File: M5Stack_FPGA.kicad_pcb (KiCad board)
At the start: 2 copper layers, 49.6 x 49.6 mm, 34 parts, among them J1 MBUS_BOTTOM, J2 MBUS_TOP, U1 BP35A1, U2 PCA9557

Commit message: Partially routed
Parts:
- removed JP1, JP2, JP3: Jumper_3_Bridged12, Jumper:SolderJumper-3_P1.3mm_Bridged12_Pad1.0x1.5mm
- added C10: 100n, Capacitor_SMD:C_0402_1005Metric, F.Cu at (36.5, 67.2)
- added C11: 100n, Capacitor_SMD:C_0402_1005Metric, F.Cu at (32.0, 67.2)
- added C13: 100n, Capacitor_SMD:C_0402_1005Metric, F.Cu at (38.5, 56.8)
- added C14: 100n, Capacitor_SMD:C_0402_1005Metric, F.Cu at (37.2, 62.2)
- added C15: 100n, Capacitor_SMD:C_0402_1005Metric, B.Cu at (29.9, 81.0)
- added C16: 100n, Capacitor_SMD:C_0402_1005Metric, F.Cu at (2.72, 27.6)
- added C17: 100n, Capacitor_SMD:C_0402_1005Metric, F.Cu at (27.8, 56.8)
- added C18: 100n, Capacitor_SMD:C_0402_1005Metric, F.Cu at (32.0, 56.8)
- added C19: 100n, Capacitor_SMD:C_0402_1005Metric, F.Cu at (26.5, 61.8)
- added C2: 4.7u, Capacitor_SMD:C_0402_1005Metric, F.Cu at (39.0, 52.2)
- added C20: 100n, Capacitor_SMD:C_0402_1005Metric, B.Cu at (24.5, 69.5)
- added C21: 4.7u, Capacitor_SMD:C_0402_1005Metric, F.Cu at (18.5, 25.0)
- added C3: 100n, Capacitor_SMD:C_0402_1005Metric, F.Cu at (26.0, 67.2)
- added C4: 100n, Capacitor_SMD:C_0402_1005Metric, F.Cu at (38.0, 67.2)
- added C5: 100n, Capacitor_SMD:C_0402_1005Metric, F.Cu at (25.8, 56.7)
- added C6: 100n, Capacitor_SMD:C_0402_1005Metric, F.Cu at (37.5, 56.8)
- added C7: 100n, Capacitor_SMD:C_0402_1005Metric, F.Cu at (6.81, 24.0)
- added C8: 100n, Capacitor_SMD:C_0402_1005Metric, F.Cu at (6.81, 25.0)
- added C9: 1u, Capacitor_SMD:C_0402_1005Metric, F.Cu at (44.0, 51.0)
- added CN1: TYPE-C-31-M-12, local:TYPE-C-31-M-12, B.Cu at (35.0, 88.0)
- added F1: 1A, Fuse:Fuse_0805_2012Metric, B.Cu at (42.0, 85.6)
- added J3: Conn_01x15_Male, Connector_PinHeader_2.54mm:PinHeader_1x15_P2.54mm_Horizontal, B.Cu at (17.9, 47.3)
- added L1: FB,600,500mA, Inductor_SMD:L_0402_1005Metric, F.Cu at (44.0, 54.2)
- added Q1: BCM857BS, Package_TO_SOT_SMD:SOT-363_SC-70-6, F.Cu at (45.5, 80.2)
- added Q2: DMG2305UX, Package_TO_SOT_SMD:SOT-23, B.Cu at (46.5, 80.2)
- added R13: 4.7k, Resistor_SMD:R_0402_1005Metric, B.Cu at (29.9, 76.0)
- added R14: NC, Resistor_SMD:R_0402_1005Metric, F.Cu at (-3.28, 37.5)
- added R15: 0, Resistor_SMD:R_0402_1005Metric, F.Cu at (6.54, 27.0)
- added R16: NC, Resistor_SMD:R_0402_1005Metric, F.Cu at (8.72, 25.0)
- added R17: 0, Resistor_SMD:R_0402_1005Metric, F.Cu at (6.54, 26.0)
- added R18: NC, Resistor_SMD:R_0402_1005Metric, F.Cu at (-5.19, 38.5)
- added R19: 0, Resistor_SMD:R_0402_1005Metric, F.Cu at (-3.28, 36.5)
- added R20: 47k, Resistor_SMD:R_0402_1005Metric, F.Cu at (4.63, 28.6)
- added R21: 5.1k, Resistor_SMD:R_0402_1005Metric, F.Cu at (22.0, 17.0)
- added R22: 5.1k, Resistor_SMD:R_0402_1005Metric, F.Cu at (4.63, 27.6)
- added R23: 10k, Resistor_SMD:R_0402_1005Metric, F.Cu at (42.8, 79.2)
- added R24: 47k, Resistor_SMD:R_0402_1005Metric, F.Cu at (42.8, 81.2)
- added TP10: TestPoint, TestPoint:TestPoint_THTPad_D1.5mm_Drill0.7mm, F.Cu at (4.58, 21.3)
- added TP11: TestPoint, TestPoint:TestPoint_THTPad_D1.5mm_Drill0.7mm, F.Cu at (25.7, 104.5)
- added TP12: TestPoint, TestPoint:TestPoint_THTPad_D1.5mm_Drill0.7mm, F.Cu at (28.2, 104.5)
- added TP13: TestPoint, TestPoint:TestPoint_THTPad_D1.5mm_Drill0.7mm, F.Cu at (-14.5, 67.5)
- added TP14: TestPoint, TestPoint:TestPoint_THTPad_D1.5mm_Drill0.7mm, F.Cu at (-14.5, 70.1)
- added TP15: TestPoint, TestPoint:TestPoint_THTPad_D1.5mm_Drill0.7mm, F.Cu at (-12.0, 67.5)
- added TP16: TestPoint, TestPoint:TestPoint_THTPad_D1.5mm_Drill0.7mm, F.Cu at (-14.5, 72.6)
- added TP17: TestPoint, TestPoint:TestPoint_THTPad_D1.5mm_Drill0.7mm, F.Cu at (-12.0, 70.1)
- added TP18: TestPoint, TestPoint:TestPoint_THTPad_D1.5mm_Drill0.7mm, F.Cu at (-9.42, 67.5)
- added TP19: TestPoint, TestPoint:TestPoint_THTPad_D1.5mm_Drill0.7mm, F.Cu at (-12.0, 72.6)
- added TP20: TestPoint, TestPoint:TestPoint_THTPad_D1.5mm_Drill0.7mm, F.Cu at (-9.42, 70.1)
- added TP21: TestPoint, TestPoint:TestPoint_THTPad_D1.5mm_Drill0.7mm, F.Cu at (-6.87, 67.5)
- added TP22: TestPoint, TestPoint:TestPoint_THTPad_D1.5mm_Drill0.7mm, F.Cu at (-9.42, 72.6)
- added TP23: TestPoint, TestPoint:TestPoint_THTPad_D1.5mm_Drill0.7mm, F.Cu at (-6.87, 70.1)
- added TP24: TestPoint, TestPoint:TestPoint_THTPad_D1.5mm_Drill0.7mm, F.Cu at (-4.32, 67.5)
- added TP25: TestPoint, TestPoint:TestPoint_THTPad_D1.5mm_Drill0.7mm, F.Cu at (-6.87, 72.6)
- added TP26: TestPoint, TestPoint:TestPoint_THTPad_D1.5mm_Drill0.7mm, F.Cu at (-4.32, 70.1)
- added TP27: TestPoint, TestPoint:TestPoint_THTPad_D1.5mm_Drill0.7mm, F.Cu at (-4.32, 72.6)
- added TP7: TestPoint, TestPoint:TestPoint_THTPad_D1.5mm_Drill0.7mm, F.Cu at (4.58, 23.8)
- added TP8: TestPoint, TestPoint:TestPoint_THTPad_D1.5mm_Drill0.7mm, F.Cu at (9.68, 21.3)
- added TP9: TestPoint, TestPoint:TestPoint_THTPad_D1.5mm_Drill0.7mm, F.Cu at (7.13, 21.3)
- added U3: MCP1700-1202E_SOT23, Package_TO_SOT_SMD:SOT-23, F.Cu at (41.5, 51.5)
- added U4: CH552T, Package_SO:TSSOP-20_4.4x6.5mm_P0.65mm, B.Cu at (34.4, 77.0)
- added X1: SG-310SCF, Crystal:Crystal_SMD_3225-4Pin_3.2x2.5mm, B.Cu at (41.0, 75.0)
- R10, R12: value 100k -> 4.7k
- U1: value BP35A1 -> GW1N-4-LQ100; footprint local:BP35A1 -> Package_QFP:LQFP-100_14x14mm_P0.5mm
- moved R1 52.6 mm to (-1.41, 46.2)
- moved R11 52.6 mm to (-0.61, 55.1)
- moved R3 52.6 mm to (-11.1, 47.0)
- moved R4 52.6 mm to (-1.41, 49.0)
- moved R5 52.6 mm to (-15.1, 47.8)
- moved R6 52.6 mm to (-15.1, 49.0)
- moved R7 52.6 mm to (-15.1, 50.1)
- moved R9 52.6 mm to (-15.1, 52.5)
- moved R10 52.6 mm to (-15.1, 53.9)
- moved R12 52.6 mm to (-0.61, 53.9)
- moved R2 52.6 mm to (0.30, 50.4)
- moved R8 52.6 mm to (-15.1, 51.4)
- moved TP3 37.4 mm to (1.19, 96.9)
- moved TP2 37.4 mm to (1.19, 94.4)
- moved TP4 37.4 mm to (1.19, 99.5)
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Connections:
- J1 pad 10: /DAC -> /F_DAC
- J1 pad 11: /SCK -> /F_SCK
- J1 pad 13: /RXD0 -> /F_RXD0
- J1 pad 14: /TXD0 -> /F_TXD0
- J1 pad 15: /RXD2 -> /F_RXD2
- J1 pad 16: /TXD2 -> /F_TXD2
- J1 pad 17: /SDA -> /F_SDA
- J1 pad 18: /SCL -> /F_SCL
- J1 pad 19: /GPIO_G2_R -> /F_GPIO_G2
- J1 pad 20: /GPIO_G5_R -> /F_GPIO_G5
- J1 pad 21: /IIS_SK -> /F_IIS_SK
- J1 pad 22: /IIS_WS -> /F_IIS_WS
- J1 pad 23: /IIS_OUT -> /F_IIS_OUT
- J1 pad 24: /IIS_MK -> /F_IIS_MK
- J1 pad 26: /IIS_IN -> /F_IIS_IN
- J1 pad 7: /MOSI -> /F_MOSI
- J1 pad 8: /DAC_SPK -> /F_DAC_SPK
- J1 pad 9: /MISO -> /F_MISO
- J2 pad 21: /IIS_WS -> /SSPI_CS_N_IIS_WS
- J2 pad 22: /IIS_SK -> /SSPI_SCLK_IIS_SK
- J2 pad 24: /IIS_OUT -> /SSPI_SO_IIS_OUT
- J2 pad 25: /IIS_IN -> /SSPI_SI_IIS_IN
- R1 pad 1: +3V3 -> Net-(R1-Pad1)
- R10 pad 1: +3V3 -> /MODE0
- R10 pad 2: /GPIO_G2_R -> GND
- R11 pad 2: /BP35_RESET -> /READY
- R12 pad 2: /BP35_WKUP -> /RECONFIG_N
- R4 pad 1: +3V3 -> Net-(R1-Pad1)
- U1 pad 1: +3V3 -> +1V2
- U1 pad 10: GND -> /SSPI_SCLK_IIS_SK
- U1 pad 11: +3V3 -> /JTAG_TDI
- U1 pad 12: GND -> /JTAG_TDO
- U1 pad 13: GND -> /FPGA_3V3
- U1 pad 14: (no net) -> /RECONFIG_N
- U1 pad 15: (no net) -> Net-(U1-Pad15)
- U1 pad 16: (no net) -> /READY
- U1 pad 17: (no net) -> /IOL11A
- U1 pad 18: (no net) -> /IOL11B
- U1 pad 19: GND -> /IOL13A
- U1 pad 20: GND -> /IOL13B
- U1 pad 3: /GPIO_G2 -> /OSC_24M
- U1 pad 4: /GPIO_G5 -> /FPGA_3V3
- U1 pad 5: /BP35_WKUP -> /PROG_RX0
- U1 pad 6: /BP35_RESET -> /IOL9A
- U1 pad 7: GND -> /IOL9B
- U1 pad 8: GND -> /JTAG_TMS
- U1 pad 9: GND -> /JTAG_TCK
- U2 pad 6: /BP35_WKUP -> /RECONFIG_N
- U2 pad 7: /BP35_RESET -> /READY
- U2 pad 9: /GPIO_G2_R -> /MODE0
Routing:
- net /FPGA_3V3: track 0.00 -> 72.8 mm, vias 0 -> 15
- net +1V2: track 0.00 -> 52.5 mm, vias 0 -> 4
- net /SSPI_SO_IIS_OUT: track 0.00 -> 50.6 mm, vias 0 -> 1
- net /SSPI_SI_IIS_IN: track 0.00 -> 48.7 mm, vias 0 -> 1
- net /GPIO_G2_R: track 47.9 -> 0.00 mm
- net /GPIO_G5_R: track 46.6 -> 0.00 mm
- net /SSPI_CS_N_IIS_WS: track 0.00 -> 43.6 mm, vias 0 -> 1
- net /SDA: track 29.0 -> 67.4 mm, vias 1 -> 5
- net GND: track 49.7 -> 13.6 mm, vias 106 -> 12
- net +3V3: track 94.6 -> 58.7 mm, vias 6 -> 3
- net /SCL: track 27.3 -> 61.6 mm, vias 1 -> 4
- net /EXT3: track 34.0 -> 0.00 mm, vias 1 -> 0
- net /EXT2: track 31.6 -> 0.00 mm, vias 1 -> 0
- net /EXT1: track 30.0 -> 0.00 mm, vias 1 -> 0
- net /EXT0: track 28.3 -> 0.00 mm, vias 1 -> 0
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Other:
- net class Default: clearance 0.2 -> 0.15
- net class UIM: clearance 0.2 -> 0.15
- rule trace_clearance: 0.2 -> 0.15
- board text removed: "3.3V"
- board text removed: "EXT0"
- board text removed: "EXT1"
- board text removed: "EXT2"
- board text removed: "EXT3"
- board text removed: "Wi-SUN Stack for M5Stack Rev.C"

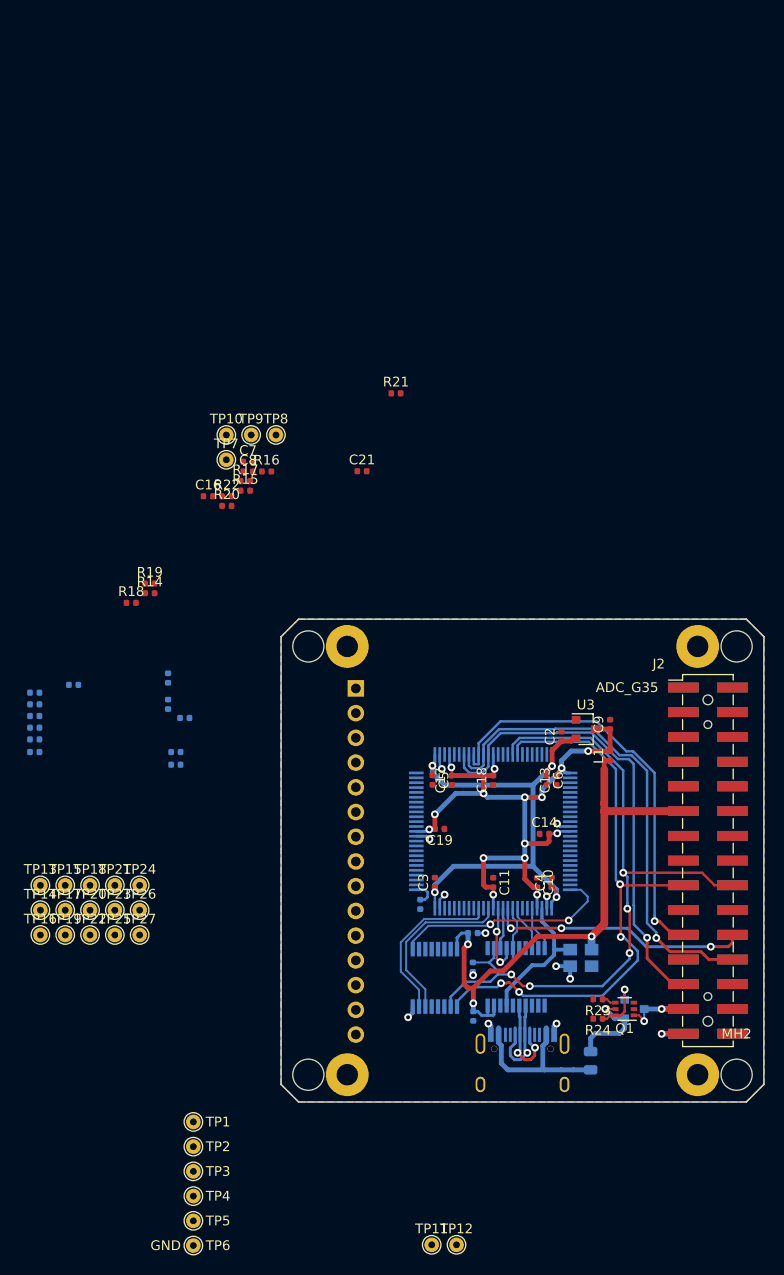
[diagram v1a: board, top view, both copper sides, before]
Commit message: Routed vital nets
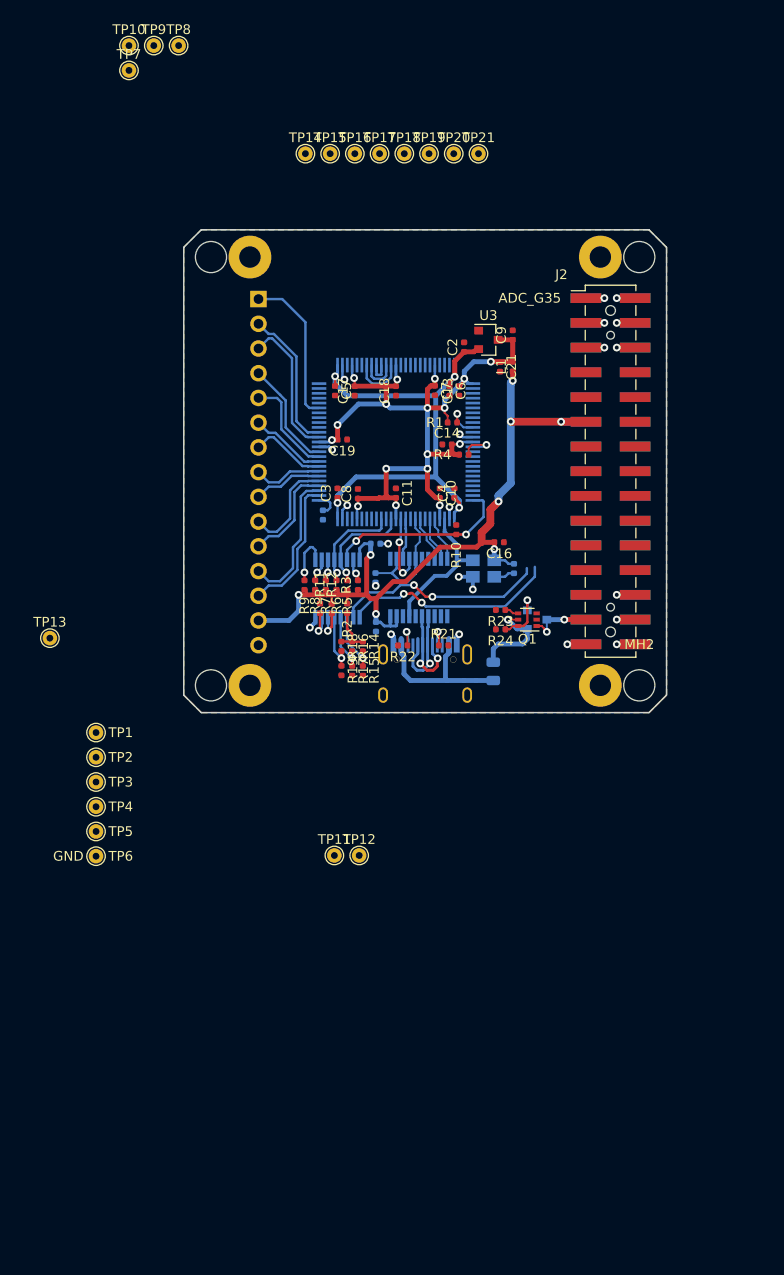
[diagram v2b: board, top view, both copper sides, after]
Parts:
- removed TP22, TP23, TP24, TP25, TP26, TP27: TestPoint, TestPoint:TestPoint_THTPad_D1.5mm_Drill0.7mm
- R1, R10, R11, R2, R3, R4, R6, R7, R8, R9: moved to F.Cu
- R12: value 4.7k -> 100k; moved to F.Cu
- R20: moved to B.Cu
- R5: value 100k -> 4.7k; moved to F.Cu
- moved TP19 88.5 mm to (25.4, -7.62)
- moved TP16 86.5 mm to (17.8, -7.62)
- moved TP20 86.2 mm to (27.9, -7.62)
- moved TP17 84.2 mm to (20.3, -7.62)
- moved TP21 83.9 mm to (30.5, -7.62)
- moved TP14 82.3 mm to (12.7, -7.62)
- moved TP18 81.8 mm to (22.9, -7.62)
- moved TP15 79.9 mm to (15.2, -7.62)
- moved R10 49.0 mm to (28.2, 31.0), turned to 90 degrees
- moved TP3 41.2 mm to (-8.81, 56.9)
- moved TP5 41.2 mm to (-8.81, 62.0)
- moved C1 41.2 mm to (19.9, 32.5)
- moved C10 41.2 mm to (26.5, 27.2)
- moved C11 41.2 mm to (22.0, 27.2)
- moved C13 41.2 mm to (28.5, 16.8)
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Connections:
- net /IOB10B renamed /IOB10_N
- CN1 pad A8: /SBU1 -> (no net)
- CN1 pad B8: /SBU2 -> (no net)
- J3 pad 1: +3V3 -> /IOB26A
- J3 pad 10: /IOB12B -> /IOB8_N
- J3 pad 11: /IOB14A -> /IOB8_P
- J3 pad 12: /IOB14B -> /IOB6_N
- J3 pad 13: /IOB19A -> /IOB6_P
- J3 pad 14: /IOB19B -> +3V3
- J3 pad 15: /IOB26A -> GND
- J3 pad 2: GND -> /IOB19_N
- J3 pad 3: /IOB6A -> /IOB19_P
- J3 pad 4: /IOB6B -> /IOB14_N
- J3 pad 5: /IOB8A -> /IOB14_P
- J3 pad 6: /IOB8B -> /IOB12_N
- J3 pad 7: /IOB10A -> /IOB12_P
- J3 pad 9: /IOB12A -> /IOB10_P
- R1 pad 1: Net-(R1-Pad1) -> /FPGA_3V3
- R1 pad 2: /SCL -> /F_SCL
- R11 pad 2: /READY -> Net-(R11-Pad2)
- R12 pad 2: /RECONFIG_N -> Net-(R12-Pad2)
- R4 pad 1: Net-(R1-Pad1) -> /FPGA_3V3
- R4 pad 2: /SDA -> /F_SDA
- R5 pad 2: /EXT3 -> /RECONFIG_N
- R6 pad 2: /EXT2 -> /READY
- R7 pad 2: /EXT1 -> Net-(R7-Pad2)
- R8 pad 2: /EXT0 -> Net-(R8-Pad2)
- R9 pad 2: /GPIO_G5_R -> Net-(R9-Pad2)
- TP1 pad 1: /EXT3 -> +5V
- TP10 pad 1: /IOB20B -> /IOB24_P
- TP11 pad 1: +3V3 -> /IOB24_N
- TP12 pad 1: +3V3 -> /IOB26B
- TP13 pad 1: +5V -> /IOB30_P
- TP14 pad 1: +3V3 -> /IOB30_N
- TP15 pad 1: GND -> /IOB32_P
- TP16 pad 1: /IOT4A -> /IOB32_N
- TP17 pad 1: /IOT4B -> /IOL9B
- TP18 pad 1: /IOT6A -> /IOL11_P
- TP19 pad 1: /IOT6B -> /IOL11_N
- TP2 pad 1: /EXT2 -> +3V3
- TP20 pad 1: /IOL9A -> /IOL13_P
- TP21 pad 1: /IOL9B -> /IOL13_N
- TP3 pad 1: /EXT1 -> GND
- TP4 pad 1: /EXT0 -> /IOB4B
- TP5 pad 1: +3V3 -> /IOB5B
- TP6 pad 1: GND -> /IOB20_P
- TP7 pad 1: /IOB4B -> +3V3
- TP8 pad 1: /IOB5B -> +3V3
- TP9 pad 1: /IOB20A -> /IOB20_N
- U1 pad 15: Net-(U1-Pad15) -> (no net)
- U1 pad 17: /IOL11A -> /IOL11_P
- U1 pad 18: /IOL11B -> /IOL11_N
- U1 pad 19: /IOL13A -> /IOL13_P
- U1 pad 20: /IOL13B -> /IOL13_N
- U1 pad 27: /IOB6A -> /IOB6_P
- U1 pad 28: /IOB6B -> /IOB6_N
- U1 pad 29: /IOB8A -> /IOB8_P
- U1 pad 30: /IOB8B -> /IOB8_N
- U1 pad 31: /IOB10A -> /IOB10_P
- U1 pad 33: /IOB12A -> /IOB12_P
- U1 pad 34: /IOB12B -> /IOB12_N
- U1 pad 35: /IOB14A -> /IOB14_P
- U1 pad 36: /IOB14B -> /IOB14_N
- U1 pad 39: /IOB19A -> /IOB19_P
- U1 pad 40: /IOB19B -> /IOB19_N
- U1 pad 41: /IOB20A -> /IOB20_P
- U1 pad 42: /IOB20B -> /IOB20_N
- U1 pad 43: /IOB24A -> /IOB24_P
- U1 pad 44: /IOB24B -> /IOB24_N
- U1 pad 46: /F_GPIO_G5 -> /IOB26B
- U1 pad 47: /F_GPIO_G2 -> /IOB30_P
- U1 pad 48: /F_IIS_WS -> /IOB30_N
- U1 pad 49: /F_IIS_SK -> /IOB32_P
- U1 pad 50: /F_IIS_MK -> /IOB32_N
- U1 pad 53: /F_IIS_OUT -> /DAC_SPK
- U1 pad 55: /F_IIS_IN -> /F_DAC_SPK
- U1 pad 56: /IIS_MK -> /MOSI
- U1 pad 6: /IOL9A -> /PROG_TX0
- U1 pad 65: /GPIO_G2 -> /F_MOSI
- U1 pad 66: /GPIO_G5 -> /DAC
- U1 pad 67: /SDA -> /F_DAC
- U1 pad 68: /SCL -> /MISO
- U1 pad 69: /RXD2 -> /F_MISO
- U1 pad 70: /TXD2 -> /SCK
- U1 pad 72: /RXD0 -> /F_SCK
- U1 pad 77: /SCK -> /F_TXD0
- U1 pad 78: /MISO -> /RXD0
- U1 pad 79: /DAC -> /F_RXD0
- U1 pad 80: /MOSI -> /TXD2
- U1 pad 81: /DAC_SPK -> /F_TXD2
- U1 pad 82: /F_DAC_SPK -> /RXD2
- U1 pad 83: /F_MOSI -> /F_RXD2
- U1 pad 84: /F_DAC -> /SCL
- U1 pad 85: /F_MISO -> /F_SCL
- U1 pad 86: /F_SCK -> /SDA
- U1 pad 89: /F_TXD0 -> /F_SDA
- U1 pad 90: /F_RXD0 -> /GPIO_G5
- U1 pad 91: /F_TXD2 -> /F_GPIO_G5
- U1 pad 92: /F_RXD2 -> /GPIO_G2
- U1 pad 93: /F_SCL -> /F_GPIO_G2
- U1 pad 94: /F_SDA -> /F_IIS_WS
- U1 pad 95: /PROG_TX0 -> /F_IIS_SK
- U1 pad 96: /IOT6B -> /IIS_MK
- U1 pad 97: /IOT6A -> /F_IIS_MK
- U1 pad 98: /IOT4B -> /F_IIS_OUT
- U1 pad 99: /IOT4A -> /F_IIS_IN
- U2 pad 10: /GPIO_G5_R -> Net-(R8-Pad2)
- U2 pad 11: /EXT0 -> Net-(R7-Pad2)
- U2 pad 12: /EXT1 -> /READY
- U2 pad 13: /EXT2 -> /RECONFIG_N
- U2 pad 14: /EXT3 -> /MODE0
- U2 pad 6: /RECONFIG_N -> Net-(R12-Pad2)
- U2 pad 7: /READY -> Net-(R11-Pad2)
- U2 pad 9: /MODE0 -> Net-(R9-Pad2)
- U4 pad 1: Net-(U4-Pad1) -> (no net)
- U4 pad 11: Net-(U4-Pad11) -> (no net)
- U4 pad 12: Net-(U4-Pad12) -> (no net)
- U4 pad 13: Net-(U4-Pad13) -> (no net)
- U4 pad 16: Net-(U4-Pad16) -> (no net)
- U4 pad 6: Net-(U4-Pad6) -> (no net)
- U4 pad 7: /PROG_SIGNAL -> (no net)
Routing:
- net /SSPI_SO_IIS_OUT: track 50.6 -> 3.98 mm, vias 1 -> 0
- net /SDA: track 67.4 -> 21.8 mm, vias 5 -> 2
- net /SSPI_SI_IIS_IN: track 48.7 -> 5.60 mm, vias 1 -> 0
- net /SSPI_CS_N_IIS_WS: track 43.6 -> 2.50 mm, vias 1 -> 0
- net /SCL: track 61.6 -> 22.2 mm, vias 4 -> 2
- net /SSPI_SCLK_IIS_SK: track 26.7 -> 0.00 mm, vias 3 -> 0
- net +3V3: track 58.7 -> 82.6 mm, vias 3 -> 8
- net /IOB26A: track 0.00 -> 15.8 mm
- net /IOB19_P: track 0.00 -> 14.8 mm
- net /IOB19_N: track 0.00 -> 14.8 mm
- net /IOB6_P: track 0.00 -> 14.3 mm
- net /IOB6_N: track 0.00 -> 14.3 mm
- net /FPGA_3V3: track 72.8 -> 85.7 mm, vias 15 -> 17
- net /HPWR: track 0.00 -> 11.3 mm, vias 0 -> 3
- net /IOB14_N: track 0.00 -> 11.2 mm
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
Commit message: Revision A Add Enclosure
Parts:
- removed TP10, TP11, TP12, TP13, TP14, TP15, TP16, TP17, TP18, TP19, TP20, TP21, TP3, TP4, TP5, TP6, TP7, TP8, TP9: TestPoint, TestPoint:TestPoint_THTPad_D1.5mm_Drill0.7mm
- added G***: LOGO, local:logo, F.Cu at (3.40, 37.6)
- TP1, TP2: footprint TestPoint:TestPoint_THTPad_D1.5mm_Drill0.7mm -> TestPoint:TestPoint_THTPad_D1.0mm_Drill0.5mm
- moved TP1 57.3 mm to (38.7, 19.9)
- moved TP2 55.1 mm to (34.1, 19.9)
- moved C7 0.29 mm to (26.0, 17.0)
- moved C13 0.25 mm to (28.5, 17.0)
- moved C6 0.25 mm to (27.5, 17.0)
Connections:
- TP1 pad 1: +5V -> +3V3
- U1 pad 17: /IOL11_P -> (no net)
- U1 pad 18: /IOL11_N -> (no net)
- U1 pad 19: /IOL13_P -> (no net)
- U1 pad 20: /IOL13_N -> (no net)
- U1 pad 22: /IOB4B -> (no net)
- U1 pad 23: /IOB5B -> (no net)
- U1 pad 41: /IOB20_P -> (no net)
- U1 pad 42: /IOB20_N -> (no net)
- U1 pad 43: /IOB24_P -> (no net)
- U1 pad 44: /IOB24_N -> (no net)
- U1 pad 46: /IOB26B -> (no net)
- U1 pad 47: /IOB30_P -> (no net)
- U1 pad 48: /IOB30_N -> (no net)
- U1 pad 49: /IOB32_P -> (no net)
- U1 pad 50: /IOB32_N -> (no net)
- U1 pad 56: /MOSI -> (no net)
- U1 pad 64: /SSPI_SCLK_IIS_SK -> /MOSI
- U1 pad 7: /IOL9B -> /SSPI_SCLK_IIS_SK
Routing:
- net /SSPI_SO_IIS_OUT: track 3.98 -> 83.6 mm, vias 0 -> 3
- net /SSPI_SI_IIS_IN: track 5.60 -> 81.6 mm, vias 0 -> 3
- net /SSPI_CS_N_IIS_WS: track 2.50 -> 76.3 mm, vias 0 -> 3
- net /F_MISO: track 0.00 -> 43.9 mm, vias 0 -> 6
- net /SDA: track 21.8 -> 60.0 mm, vias 2 -> 3
- net /DAC_SPK: track 0.00 -> 34.1 mm, vias 0 -> 1
- net /F_SCK: track 0.00 -> 33.9 mm
- net /F_DAC_SPK: track 0.00 -> 33.3 mm, vias 0 -> 2
- net /SSPI_SCLK_IIS_SK: track 0.00 -> 32.9 mm, vias 0 -> 3
- net /MOSI: track 0.00 -> 32.3 mm, vias 0 -> 1
- net /DAC: track 0.00 -> 32.2 mm, vias 0 -> 3
- net /F_MOSI: track 0.00 -> 31.4 mm, vias 0 -> 2
- net /SCK: track 0.00 -> 30.1 mm, vias 0 -> 1
- net /MISO: track 0.00 -> 29.0 mm, vias 0 -> 1
- net /SCL: track 22.2 -> 50.9 mm, vias 2 -> 5
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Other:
- net class Default: trace_width 0.25 -> 0.2
- board text added: "M5Stack FPGA Board Rev.A 2020-01-16 Kenta IDA (@ciniml)"
- board text removed: "GND"
